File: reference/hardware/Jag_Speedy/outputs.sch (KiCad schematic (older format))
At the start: 8 parts, among them IC11 VNS3NV04DP-E, Q1 SSM3K357R,LF, Q2 SSM3K357R,LF, Q3 SSM3K357R,LF

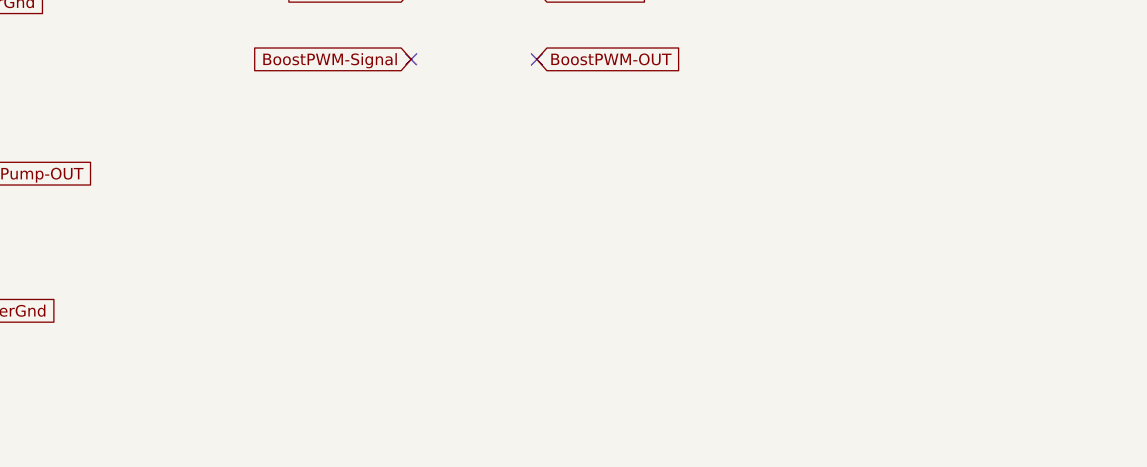
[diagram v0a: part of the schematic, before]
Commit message: Added Water Pump PWM
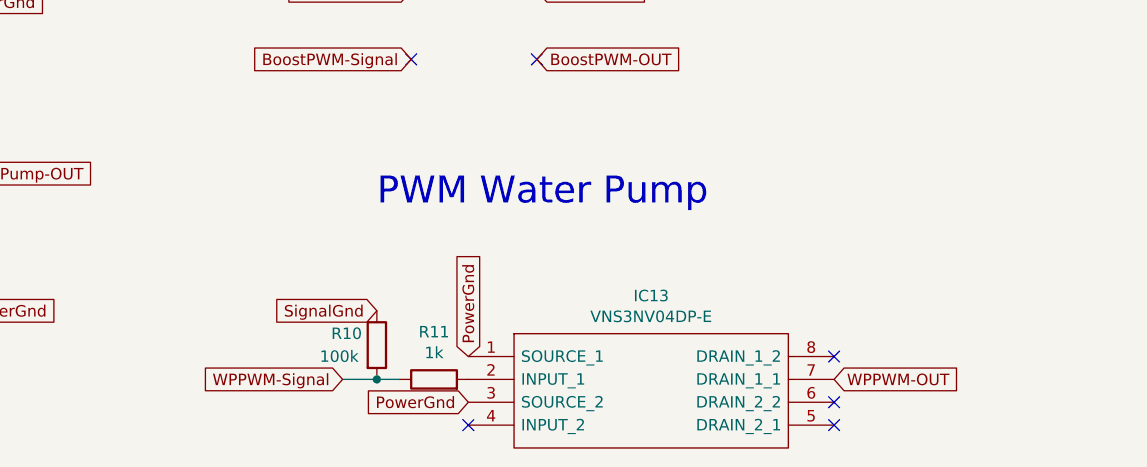
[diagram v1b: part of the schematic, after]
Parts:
- added IC13: VNS3NV04DP-E, Package_SO:SO-8_3.9x4.9mm_P1.27mm, symbol Jag_Speedy-rescue:VNS3NV04DP-E-VNS3NV04DP-E-Jag_Speedy-rescue
- added R10: 100k, Resistor_SMD:R_0805_2012Metric, symbol Device:R
- added R11: 1k, Resistor_SMD:R_0805_2012Metric, symbol Device:R
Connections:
- net PowerGnd: now also IC13.1 (SOURCE_1), IC13.3 (SOURCE_2)
- net SignalGnd: now also R10.1
- new net: IC13.2 (INPUT_1), R11.2
- new net WPPWM-OUT: IC13.7 (DRAIN_1_1)
- new net WPPWM-Signal: R10.2, R11.1
- no-connect marks 6 -> 10
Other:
- note added: "PWM Water Pump"
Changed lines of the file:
@@
 Text GLabel 4250 1400 0    50   Input ~ 0
 SignalGnd
+Text Notes 4200 3800 0    118  ~ 0
+PWM Water Pump
+$Comp
+L Jag_Speedy-rescue:VNS3NV04DP-E-VNS3NV04DP-E-Jag_Speedy-rescue IC?
+U 1 1 5F1F22C8
+P 4600 4450
+AR Path="/5EF090BF/5F1F22C8" Ref="IC?"  Part="1"
+AR Path="/5F198969/5F1F22C8" Ref="IC13"  Part="1"
+F 0 "IC13" H 5400 4715 50  0000 C CNN
+F 1 "VNS3NV04DP-E" H 5400 4624 50  0000 C CNN
+F 2 "Package_SO:SO-8_3.9x4.9mm_P1.27mm" H 6050 4550 50  0001 L CNN
+F 3 "https://www.st.com/resource/en/datasheet/vns3nv04dp-e.pdf" H 6050 4450 50  0001 L CNN
+F 4 "STMicroelectronics VNS3NV04DP-E Load Switch IC, 8-Pin, SOIC" H 6050 4350 50  0001 L CNN "Description"
+F 5 "1.75" H 6050 4250 50  0001 L CNN "Height"
+F 6 "STMicroelectronics" H 6050 4150 50  0001 L CNN "Manufacturer_Name"
+F 7 "VNS3NV04DP-E" H 6050 4050 50  0001 L CNN "Manufacturer_Part_Number"
+F 8 "VNS3NV04DP-E" H 6050 3950 50  0001 L CNN "Arrow Part Number"
+F 9 "https://www.arrow.com/en/products/vns3nv04dp-e/stmicroelectronics" H 6050 3850 50  0001 L CNN "Arrow Price/Stock"
+F 10 "511-VNS3NV04DP-E" H 6050 3750 50  0001 L CNN "Mouser Part Number"
+F 11 "https://www.mouser.com/Search/Refine.aspx?Keyword=511-VNS3NV04DP-E" H 6050 3650 50  0001 L CNN "Mouser Price/Stock"
+	1    4600 4450
+	1    0    0    -1
+$EndComp
+Text GLabel 4600 4650 0    50   Input ~ 0
+PowerGnd
+Text GLabel 4600 4450 1    50   Input ~ 0
+PowerGnd
+Text GLabel 6200 4550 2    50   Input ~ 0
+WPPWM-OUT
+Connection ~ 4200 4550
+Wire Wire Line
+	4200 4550 4300 4550
+Wire Wire Line
+	4200 4550 4050 4550
+$Comp
+L Device:R R11
+U 1 1 5F1F22E4
+P 4450 4550
+F 0 "R11" V 4657 4550 50  0000 C CNN
+F 1 "1k" V 4566 4550 50  0000 C CNN
+F 2 "Resistor_SMD:R_0805_2012Metric" V 4380 4550 50  0001 C CNN
+F 3 "~" H 4450 4550 50  0001 C CNN
+	1    4450 4550
+	0    -1   -1   0
+$EndComp
+$Comp
+L Device:R R10
+U 1 1 5F1F22EA
+P 4200 4400
+F 0 "R10" H 4000 4450 50  0000 L CNN
+F 1 "100k" H 3950 4350 50  0000 L CNN
+F 2 "Resistor_SMD:R_0805_2012Metric" V 4130 4400 50  0001 C CNN
+F 3 "~" H 4200 4400 50  0001 C CNN
+	1    4200 4400
+	1    0    0    -1
+$EndComp
+Text GLabel 4050 4550 0    50   Input ~ 0
+WPPWM-Signal
+NoConn ~ 6200 4650
+NoConn ~ 6200 4450
+Text GLabel 4200 4250 0    50   Input ~ 0
+SignalGnd
+NoConn ~ 6200 4750
+NoConn ~ 4600 4750
 $EndSCHEMATC
